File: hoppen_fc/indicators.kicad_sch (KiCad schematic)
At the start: 18 parts, among them Q1 PMBT3904YS, U9 74AHCT1G125

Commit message: work
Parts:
- D4, D5, D6, D7: footprint 0_indicators:LED_SK6812_PLCC4_5.0x5.0mm_P3.2mm -> 0_indicators:LED-SMD_4P-L2.0-W2.0-BR; LCSC (none) -> C2909058
- U9: footprint Package_TO_SOT_SMD:SOT-353_SC-70-5 -> 0_transceivers:SOT-23-5
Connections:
- net +5V: now also D4.1 (VDD), D5.1 (VDD), D6.1 (VDD), D7.1 (VDD); no longer D4.3 (VDD), D5.3 (VDD), D6.3 (VDD), D7.3 (VDD)
- net ADD_LED_D_0: now also D4.4 (DIN); no longer D4.2 (DIN)
- net ADD_LED_D_1: now also D4.2 (DOUT), D5.4 (DIN); no longer D4.4 (DOUT), D5.2 (DIN)
- net ADD_LED_D_2: now also D5.2 (DOUT), D6.4 (DIN); no longer D5.4 (DOUT), D6.2 (DIN)
- net ADD_LED_D_3: now also D6.2 (DOUT), D7.4 (DIN); no longer D6.4 (DOUT), D7.2 (DIN)
- net GND: now also D4.3 (GND), D5.3 (GND), D6.3 (GND), D7.3 (GND); no longer D4.1 (VSS), D5.1 (VSS), D6.1 (VSS), D7.1 (VSS)
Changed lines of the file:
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@@
 			)
 		)
-		(property "Footprint" "0_indicators:LED_SK6812_PLCC4_5.0x5.0mm_P3.2mm"
+		(property "Footprint" "0_indicators:LED-SMD_4P-L2.0-W2.0-BR"
 			(at 161.29 115.57 0)
 			(effects
@@
 			)
 		)
-		(property "Datasheet" "https://cdn-shop.adafruit.com/product-files/1138/SK6812+LED+datasheet+.pdf"
+		(property "Datasheet" "https://jlcpcb.com/api/file/downloadByFileSystemAccessId/8589835384537849856"
 			(at 146.05 119.38 0)
 			(effects
@@
 			)
 		)
+		(property "LCSC" "C2909058"
+			(at 185.42 122.428 0)
+			(effects
+				(font
+					(size 1.27 1.27)
+				)
+				(hide yes)
+			)
+		)
 		(pin "2"
 		)
@@
 			)
 		)
-		(property "Footprint" "0_indicators:LED_SK6812_PLCC4_5.0x5.0mm_P3.2mm"
+		(property "Footprint" "0_indicators:LED-SMD_4P-L2.0-W2.0-BR"
 			(at 110.49 115.57 0)
 			(effects
@@
 			)
 		)
-		(property "Datasheet" "https://cdn-shop.adafruit.com/product-files/1138/SK6812+LED+datasheet+.pdf"
+		(property "Datasheet" "https://jlcpcb.com/api/file/downloadByFileSystemAccessId/8589835384537849856"
 			(at 95.25 119.38 0)
 			(effects
@@
 			)
 		)
+		(property "LCSC" "C2909058"
+			(at 134.62 122.428 0)
+			(effects
+				(font
+					(size 1.27 1.27)
+				)
+				(hide yes)
+			)
+		)
 		(pin "2"
 		)
@@
 		(fields_autoplaced yes)
 		(property "Reference" "U9"
-			(at 107.95 130.7398 0)
+			(at 393.7 542.2198 0)
 			(effects
 				(font
@@
 		)
 		(property "Value" "74AHCT1G125"
-			(at 107.95 133.2798 0)
-			(effects
-				(font
-					(size 1.27 1.27)
-				)
-			)
-		)
-		(property "Footprint" "Package_TO_SOT_SMD:SOT-353_SC-70-5"
-			(at 95.25 137.16 0)
-			(effects
-				(font
-					(size 1.27 1.27)
-				)
-				(hide yes)
-			)
-		)
-		(property "Datasheet" "http://www.ti.com/lit/sg/scyt129e/scyt129e.pdf"
-			(at 95.25 110.49 0)
+			(at 393.7 544.7598 0)
+			(effects
+				(font
+					(size 1.27 1.27)
+				)
+			)
+		)
+		(property "Footprint" "0_transceivers:SOT-23-5"
+			(at 381 548.64 0)
+			(effects
+				(font
+					(size 1.27 1.27)
+				)
+				(hide yes)
+			)
+		)
+		(property "Datasheet" "https://jlcpcb.com/api/file/downloadByFileSystemAccessId/8590923861753999360"
+			(at 381 521.97 0)
 			(effects
 				(font
@@
 		)
 		(property "Description" "Single Buffer Gate Tri-State, Low-Voltage CMOS"
-			(at 95.25 113.03 0)
+			(at 381 524.51 0)
 			(effects
 				(font
@@
 		(instances
 			(project ""
-				(path "/abe950a1-9eef-4508-9fd4-31d3e723e029/c85454e5-a89e-41eb-a5ed-71b4fc4cf13a/8b8c6acc-be78-4f0d-9edb-cfc9fd9bc6b4"
+				(path "/abe950a1-9eef-4508-9fd4-31d3e723e029/c85454e5-a89e-41eb-a5ed-71b4fc4cf13a"
+					(reference "U9")
+					(unit 1)
+				)
+				(path "/abe950a1-9eef-4508-9fd4-31d3e723e029/c85454e5-a89e-41eb-a5ed-71b4fc4cf13a/8b8c6acc-be78-4f0d-9edb-cfc9fd9bc6b4"
+					(reference "U9")
+					(unit 1)
+				)
+				(path "/abe950a1-9eef-4508-9fd4-31d3e723e029/c85454e5-a89e-41eb-a5ed-71b4fc4cf13a/b2889d66-ad44-4386-8a59-32f6d6b6b256"
 					(reference "U9")
 					(unit 1)
@@
 			)
 		)
-		(property "Footprint" "0_indicators:LED_SK6812_PLCC4_5.0x5.0mm_P3.2mm"
+		(property "Footprint" "0_indicators:LED-SMD_4P-L2.0-W2.0-BR"
 			(at 135.89 115.57 0)
 			(effects
@@
 			)
 		)
-		(property "Datasheet" "https://cdn-shop.adafruit.com/product-files/1138/SK6812+LED+datasheet+.pdf"
+		(property "Datasheet" "https://jlcpcb.com/api/file/downloadByFileSystemAccessId/8589835384537849856"
 			(at 120.65 119.38 0)
 			(effects
@@
 			)
 		)
+		(property "LCSC" "C2909058"
+			(at 160.02 122.428 0)
+			(effects
+				(font
+					(size 1.27 1.27)
+				)
+				(hide yes)
+			)
+		)
 		(pin "2"
 		)
@@
 			)
 		)
-		(property "Footprint" "0_indicators:LED_SK6812_PLCC4_5.0x5.0mm_P3.2mm"
+		(property "Footprint" "0_indicators:LED-SMD_4P-L2.0-W2.0-BR"
 			(at 186.69 115.57 0)
 			(effects
@@
 			)
 		)
-		(property "Datasheet" "https://cdn-shop.adafruit.com/product-files/1138/SK6812+LED+datasheet+.pdf"
+		(property "Datasheet" "https://jlcpcb.com/api/file/downloadByFileSystemAccessId/8589835384537849856"
 			(at 171.45 119.38 0)
 			(effects
@@
 			(effects
 				(font
+					(size 1.27 1.27)
+				)
+				(hide yes)
+			)
+		)
+		(property "LCSC" "C2909058"
+			(at 210.82 122.428 0)
+			(effects
+				(font

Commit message: finished adding lcsc numbers
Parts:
- removed C45: 4u7, 0_resistor_smd:R_0603_1608Metric, symbol Device:C
- removed Q1: PMBT3904YS, 0_transistors:SOT-363_SC-70-6, symbol 0_transistors:PMBT3904YS
- added C101: 1u, 0_capacitor_smd:C_0603_1608Metric, symbol Device:C
- added D7: 1N4148W, Diode_SMD:D_SOD-123, symbol Diode:1N4148W
- added Q2: MMBT3904, Package_TO_SOT_SMD:SOT-23, symbol Transistor_BJT:MMBT3904
- B1: value ~ -> FUET-5030
- C102: renamed from C46; LCSC (none) -> C307331
- C103: renamed from C47; LCSC (none) -> C307331
- C104: renamed from C48; LCSC (none) -> C307331
- C105: renamed from C49; LCSC (none) -> C307331
- D8: renamed from D2; value Green -> GREEN 0805; footprint 0_diodes:LED_0402_1005Metric -> 0_diodes:LED_0805_2012Metric; LCSC (none) -> C2297
- D9: renamed from D3; value Blue -> BLUE 0805; footprint 0_diodes:LED_0402_1005Metric -> 0_diodes:LED_0805_2012Metric; LCSC C22355736 -> C84256
- R47: renamed from R17; LCSC (none) -> C11702
- R48: renamed from R19; value 1k -> 220R; LCSC (none) -> C25091
- R49: renamed from R18; LCSC (none) -> C11702
- R50: renamed from R23; LCSC (none) -> C25744
- U17: renamed from U9; LCSC (none) -> C20617903
- renumbered D4 to D10, D5 to D11, D6 to D12, D7 to D13
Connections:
- net +3V3: now also C101.1, D7.1 (K)
- net BUZZER_BASE: now also Q2.1 (B)
- net BUZZER_N: now also D7.2 (A), Q2.3 (C)
- net GND: now also C101.2, Q2.2 (E)

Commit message: ready for routing?
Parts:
- added R51: 22R, 0_resistor_smd:R_0402_1005Metric, symbol Device:R
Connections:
- net ADD_LED_D_0: now also R51.2; no longer U17.4
- new net PRE_ADD_LED_D_0: R51.1, U17.4
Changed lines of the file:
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@@
 	(wire
 		(pts
-			(xy 114.3 137.16) (xy 114.3 144.78)
+			(xy 116.84 137.16) (xy 116.84 144.78)
 		)
 		(stroke
@@
 	(wire
 		(pts
-			(xy 102.87 137.16) (xy 114.3 137.16)
-		)
-		(stroke
-			(width 0)
-			(type default)
-		)
-	)
-	(wire
-		(pts
 			(xy 90.17 144.78) (xy 90.17 149.86)
 		)
@@
 	(wire
 		(pts
-			(xy 114.3 144.78) (xy 127 144.78)
+			(xy 116.84 144.78) (xy 127 144.78)
+		)
+		(stroke
+			(width 0)
+			(type default)
+		)
+	)
+	(wire
+		(pts
+			(xy 102.87 137.16) (xy 109.22 137.16)
 		)
 		(stroke
@@
 			(font
 				(size 0.635 0.635)
+			)
+			(justify left bottom)
+		)
+	)
+	(label "PRE_ADD_LED_D_0"
+		(at 102.87 137.16 0)
+		(effects
+			(font
+				(size 0.508 0.508)
 			)
 			(justify left bottom)
@@
 			)
 		)
+		(property "Sim.Device" "NPN"
+			(at 184.15 88.9 0)
+			(effects
+				(font
+					(size 1.27 1.27)
+				)
+				(hide yes)
+			)
+		)
+		(property "Sim.Pins" "1=B 2=E 3=C"
+			(at 184.15 88.9 0)
+			(effects
+				(font
+					(size 1.27 1.27)
+				)
+				(hide yes)
+			)
+		)
 		(pin "2"
 		)
@@
 					(unit 1)
 				)
+			)
+		)
+	)
+	(symbol
+		(lib_id "Device:R")
+		(at 113.03 137.16 90)
+		(unit 1)
+		(exclude_from_sim no)
+		(in_bom yes)
+		(on_board yes)
+		(dnp no)
+		(property "Reference" "R51"
+			(at 113.03 142.24 90)
+			(effects
+				(font
+					(size 1.27 1.27)
+				)
+			)
+		)
+		(property "Value" "22R"
+			(at 113.03 139.7 90)
+			(effects
+				(font
+					(size 1.27 1.27)
+				)
+			)
+		)
+		(property "Footprint" "0_resistor_smd:R_0402_1005Metric"
+			(at 113.03 138.938 90)
+			(effects
+				(font
+					(size 1.27 1.27)
+				)
+				(hide yes)
+			)
+		)
+		(property "Datasheet" "~"
+			(at 113.03 137.16 0)
+			(effects
+				(font
+					(size 1.27 1.27)
+				)
+				(hide yes)
+			)
+		)
+		(property "Description" "Resistor"
+			(at 113.03 137.16 0)
+			(effects
+				(font
+					(size 1.27 1.27)
+				)
+				(hide yes)
+			)
+		)
+		(property "LCSC" "C25092"
+			(at 113.03 137.16 90)
+			(effects
+				(font
+					(size 1.27 1.27)
+				)
+				(hide yes)
+			)
+		)
+		(pin "1"
+		)
+		(pin "2"
+		)
+		(instances
+			(project "hoppen_fc"
+				(path "/abe950a1-9eef-4508-9fd4-31d3e723e029/c85454e5-a89e-41eb-a5ed-71b4fc4cf13a/8b8c6acc-be78-4f0d-9edb-cfc9fd9bc6b4"
+					(reference "R51")
+					(unit 1)
+				)

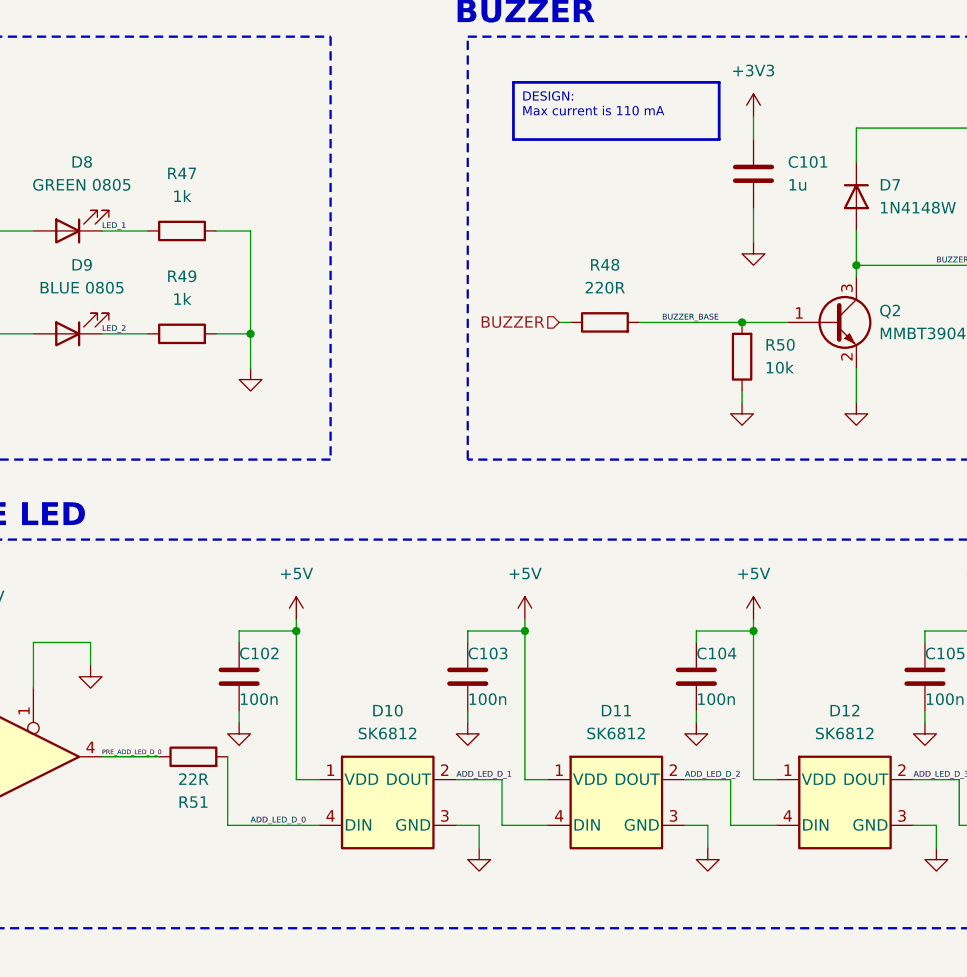
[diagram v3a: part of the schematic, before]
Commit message: routing and adding rf module
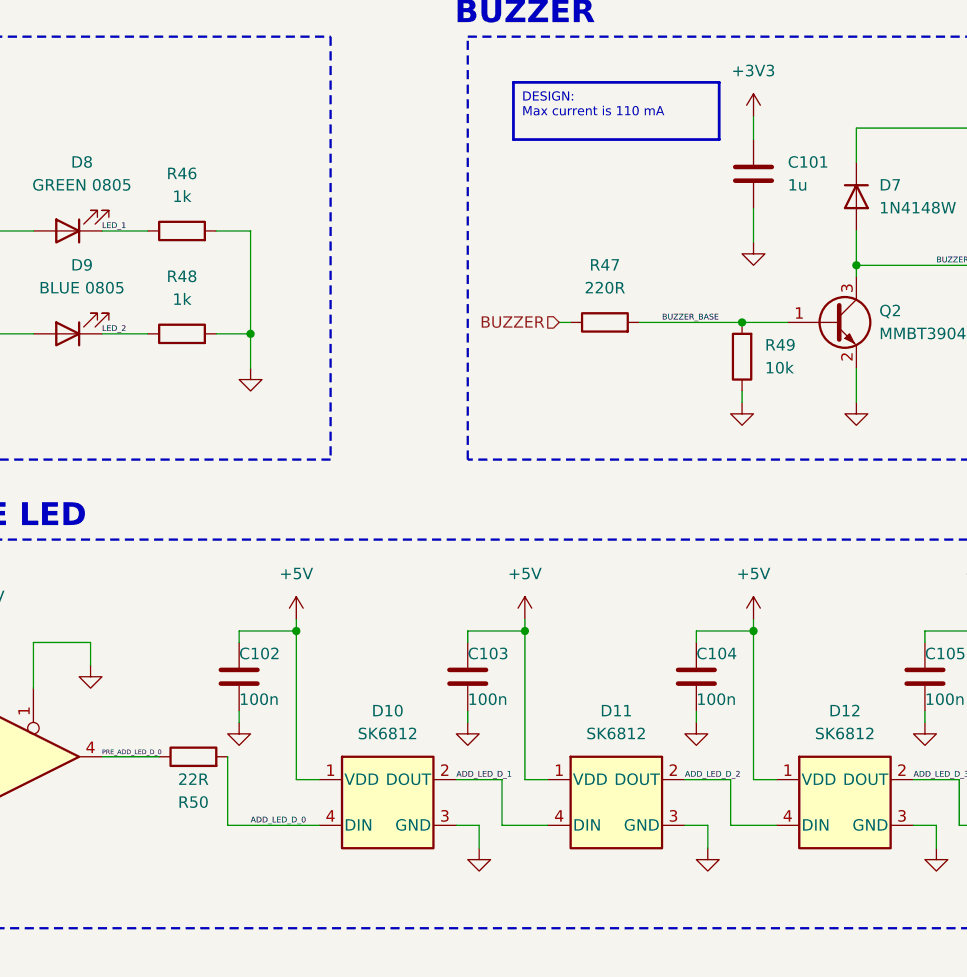
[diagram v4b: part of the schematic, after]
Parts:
- renumbered R47 to R46, R48 to R47, R49 to R48, R50 to R49, R51 to R50
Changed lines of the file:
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@@
 		(dnp no)
 		(fields_autoplaced yes)
-		(property "Reference" "R48"
+		(property "Reference" "R47"
 			(at 158.75 82.55 90)
 			(effects
@@
 			(project "hoppen_fc"
 				(path "/abe950a1-9eef-4508-9fd4-31d3e723e029/c85454e5-a89e-41eb-a5ed-71b4fc4cf13a/8b8c6acc-be78-4f0d-9edb-cfc9fd9bc6b4"
-					(reference "R48")
+					(reference "R47")
 					(unit 1)
 				)
@@
 		(dnp no)
 		(fields_autoplaced yes)
-		(property "Reference" "R47"
+		(property "Reference" "R46"
 			(at 111.76 72.39 90)
 			(effects
@@
 			(project "hoppen_fc"
 				(path "/abe950a1-9eef-4508-9fd4-31d3e723e029/c85454e5-a89e-41eb-a5ed-71b4fc4cf13a/8b8c6acc-be78-4f0d-9edb-cfc9fd9bc6b4"
-					(reference "R47")
+					(reference "R46")
 					(unit 1)
 				)
@@
 		(on_board yes)
 		(dnp no)
-		(property "Reference" "R51"
+		(property "Reference" "R50"
 			(at 113.03 142.24 90)
 			(effects
@@
 			(project "hoppen_fc"
 				(path "/abe950a1-9eef-4508-9fd4-31d3e723e029/c85454e5-a89e-41eb-a5ed-71b4fc4cf13a/8b8c6acc-be78-4f0d-9edb-cfc9fd9bc6b4"
-					(reference "R51")
+					(reference "R50")
 					(unit 1)
 				)
@@
 		(dnp no)
 		(fields_autoplaced yes)
-		(property "Reference" "R50"
+		(property "Reference" "R49"
 			(at 176.53 91.4399 0)
 			(effects
@@
 			(project "hoppen_fc"
 				(path "/abe950a1-9eef-4508-9fd4-31d3e723e029/c85454e5-a89e-41eb-a5ed-71b4fc4cf13a/8b8c6acc-be78-4f0d-9edb-cfc9fd9bc6b4"
-					(reference "R50")
+					(reference "R49")
 					(unit 1)
 				)
@@
 		(dnp no)
 		(fields_autoplaced yes)
-		(property "Reference" "R49"
+		(property "Reference" "R48"
 			(at 111.76 83.82 90)
 			(effects
@@
 			(project "hoppen_fc"
 				(path "/abe950a1-9eef-4508-9fd4-31d3e723e029/c85454e5-a89e-41eb-a5ed-71b4fc4cf13a/8b8c6acc-be78-4f0d-9edb-cfc9fd9bc6b4"
-					(reference "R49")
-					(unit 1)
-				)
+					(reference "R48")
+					(unit 1)
+				)

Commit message: bump
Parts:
- renumbered C101 to C77, C102 to C78, C103 to C79, C104 to C80, C105 to C81, D11 to D10, D12 to D11, D13 to D12, D7 to D6, D8 to D7, D9 to D8, D10 to D9, R46 to R31, R47 to R32, R48 to R33, R49 to R34, R50 to R35, U17 to U15

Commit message: bump
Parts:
- removed C77: 1u, 0_capacitor_smd:C_0603_1608Metric, symbol Device:C
- added C64: 10u, 0_capacitor_smd:C_0805_2012Metric, symbol Device:C
- Q2: LCSC C239187 -> C7420353
- R34: renamed from R31; LCSC C11702 -> C106235
- R36: renamed from R33; LCSC C11702 -> C106235
- R38: renamed from R35; LCSC C25092 -> C2929994
- renumbered C78 to C65, C79 to C66, C80 to C67, C81 to C68, R32 to R35, R34 to R37, U15 to U17
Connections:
- net +3V3: now also C64.1
- net GND: now also C64.2
